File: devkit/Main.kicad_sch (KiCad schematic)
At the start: 49 parts, among them IC101 MAX32664, IC102 MCP73832-2-OT, IC103 MAX86141, IC104 LIS2DS12, IC105 MIC5365-1.8, IC106 TPS61240, J101 I2C, J102 SPI, M101 BM15C, Q101 BSS138, SW101 RESET, SW102 BTN1, X101 CHARGE, X102 DEBUG, X103 BATTERY, Y101 32kHz

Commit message: Switch to new KiCad template, fixing CI/CD
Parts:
- C105, C110, C115, C118: symbol Device:C -> Device:C_Small
- IC105: manf# MIC5365-1.8YD5-TR -> MIC5365-1.8YD5-TR
- LED101: value SFH 7016 -> SFH7016
- R101: footprint Capacitor_SMD:C_0603_1608Metric -> Resistor_SMD:R_0402_1005Metric
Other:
- note removed: "Layout guidelines for MAX8614x: - Connect all GNDs to a single ground plane and use one single via to PCB ground - Use different vias for all decoupling caps - PD_IN must be shielded by PD_GND - PD_GND on the layer where the MAX8614x is mounted, PG_IN under PD_GND - No traces over or under PD_GND"
- moved on the sheet: C101, C102, C103, C104, C105, C106, C107, C108, C109, C110, C111, C112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

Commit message: Issue #11
Signed-off-by: Daniel Kampert <DanielKampert@kampis-elektroecke.de>
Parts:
- D102, D103: value D_Photo -> VEMD8082
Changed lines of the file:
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@@
 			)
 		)
-		(property "Value" "D_Photo"
+		(property "Value" "VEMD8082"
 			(at 340.6775 82.55 0)
 			(effects
@@
 			)
 		)
-		(property "Value" "D_Photo"
+		(property "Value" "VEMD8082"
 			(at 340.6775 68.58 0)
 			(effects

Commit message: doc: Update documentation
- Update README
- Update ref designators
- Update CI/CD pipeline

Signed-off-by: Daniel Kampert <DanielKampert@kampis-elektroecke.de>
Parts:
- R401: renamed from R101; symbol Device:R -> Device:R_Small
- R403: renamed from R103; symbol Device:R -> Device:R_Small
- R406: renamed from R108; symbol Device:R -> Device:R_Small
- R407: renamed from R109; symbol Device:R -> Device:R_Small
- R409: renamed from R107; symbol Device:R -> Device:R_Small
- R410: renamed from R110; symbol Device:R -> Device:R_Small; now in the parts list
- renumbered C114 to C401, C115 to C402, C117 to C403, C118 to C404, C105 to C405, C101 to C406, C110 to C407, C102 to C408, C103 to C409, C104 to C410, C106 to C411, C107 to C412, C108 to C413, C109 to C414, C111 to C415, C112 to C416, C113 to C417, C116 to C418, D101 to D401, D102 to D402, D103 to D403, IC105 to IC401, IC106 to IC402, IC102 to IC403, IC101 to IC404, IC103 to IC405, IC104 to IC406, J101 to J401, J102 to J402, L101 to L401, LED101 to LED401, M101 to M401, Q101 to Q401, R102 to R402, R105 to R404, R106 to R405, R104 to R408, SW101 to SW401, SW102 to SW402, X101 to X401, X103 to X402, X102 to X403, Y101 to Y401
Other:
- moved on the sheet: R403

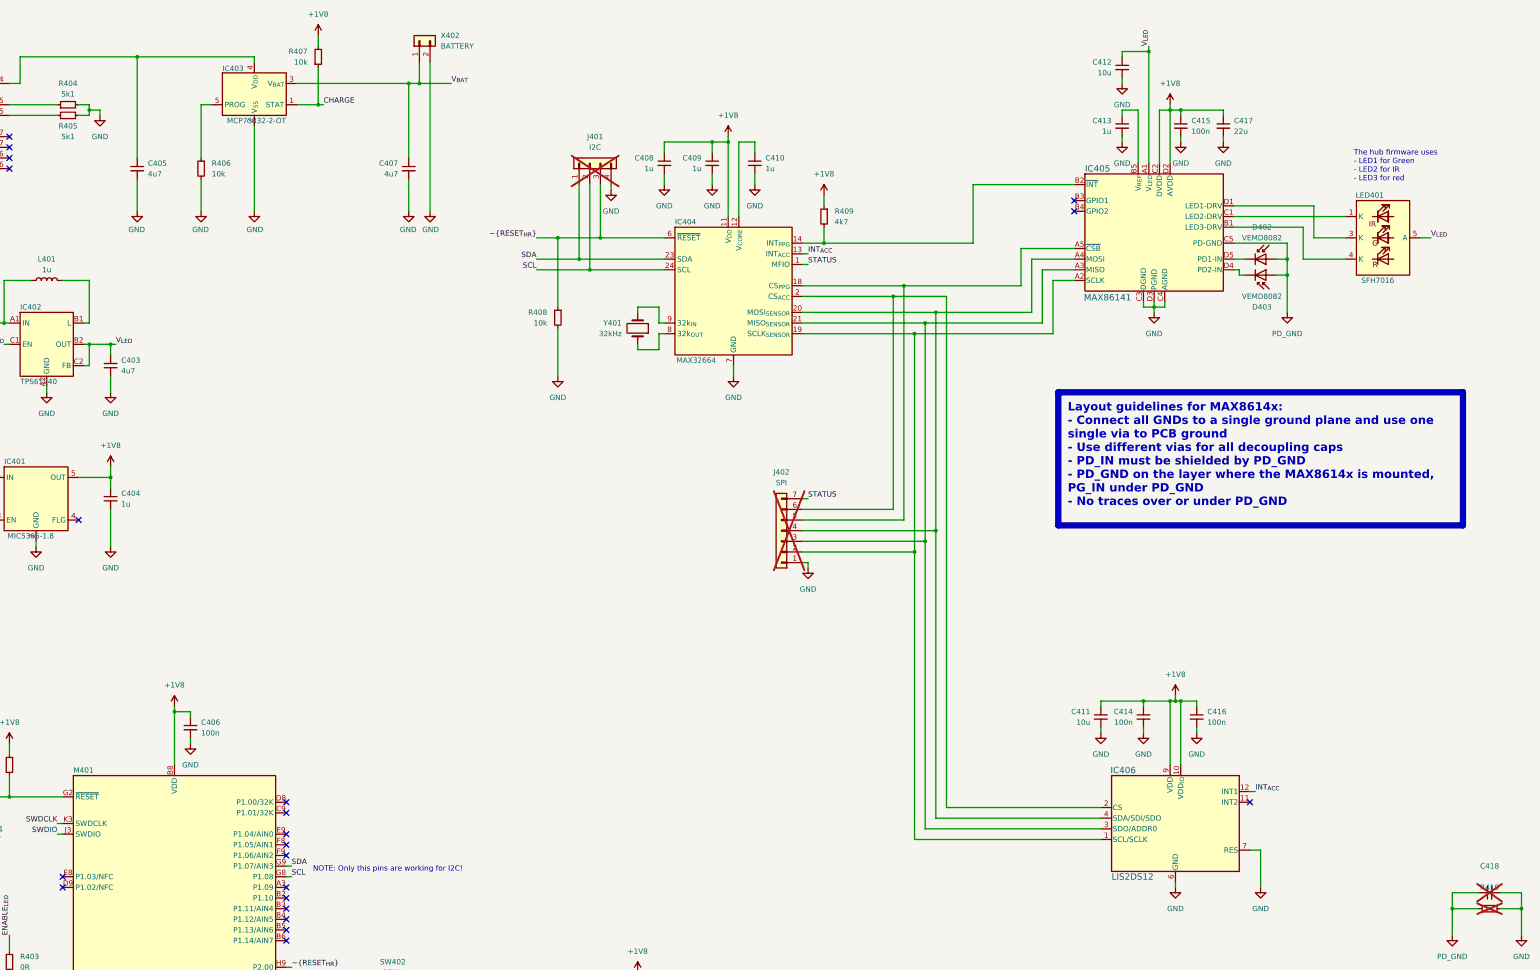
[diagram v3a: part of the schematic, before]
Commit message: Prepare release
- Set variant to CHECKED
- Remove unused files
- Fix ERC errors
- Fix DRC errors
- Fix different documentation errors
- Fix different path errors for the release build
- Remove Power Sequencing page
- Add PDF_REPORT_ROOT_DIR variable to build
- Add script for CHANGELOG generation

Signed-off-by: Daniel Kampert <DanielKampert@kampis-elektroecke.de>
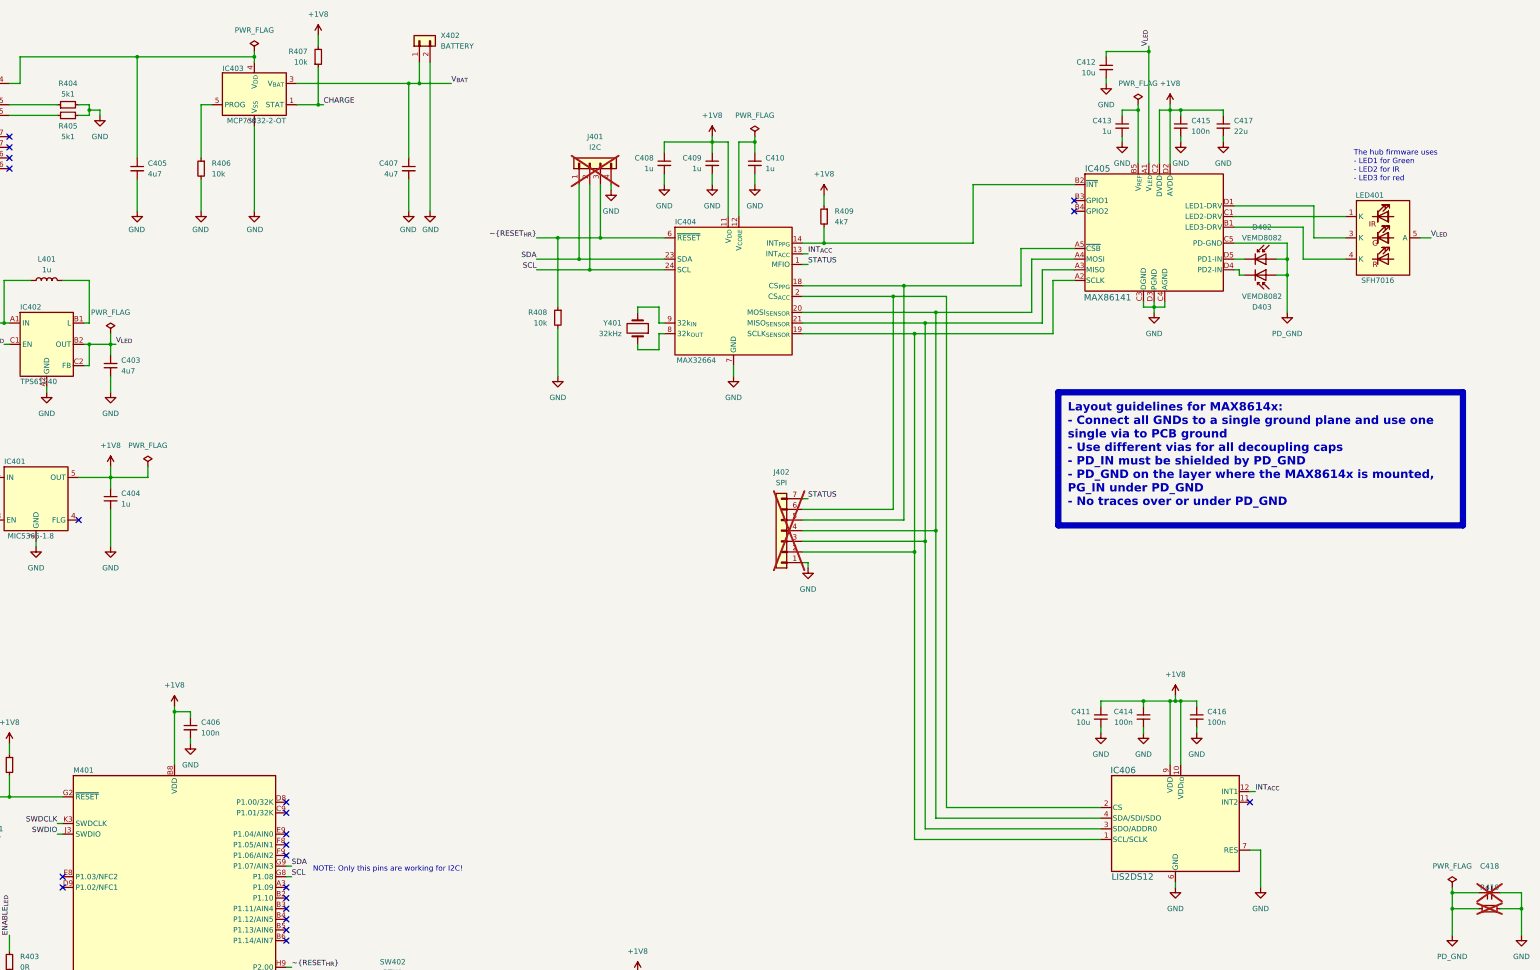
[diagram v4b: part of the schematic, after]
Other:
- moved on the sheet: C412
